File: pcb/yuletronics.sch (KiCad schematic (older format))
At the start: 35 parts, among them IC1 STM32F042F6P6, IC2 MCP1700, IC3 TLV61225, J1 BATT, J2 MICROUSB, P1 SWD_TC, SW1 BOOTLOAD, SW2 PWR_SWITCH

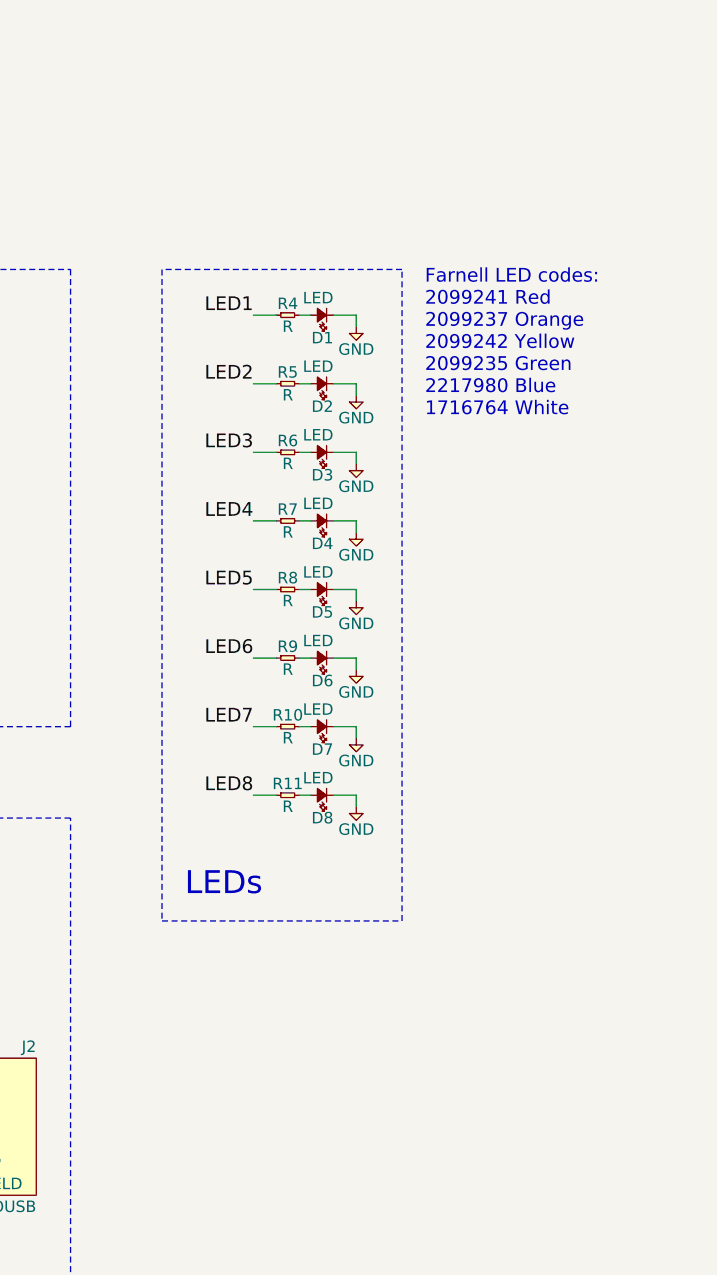
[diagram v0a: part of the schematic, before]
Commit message: More LEDs, MOSFETs, board outline
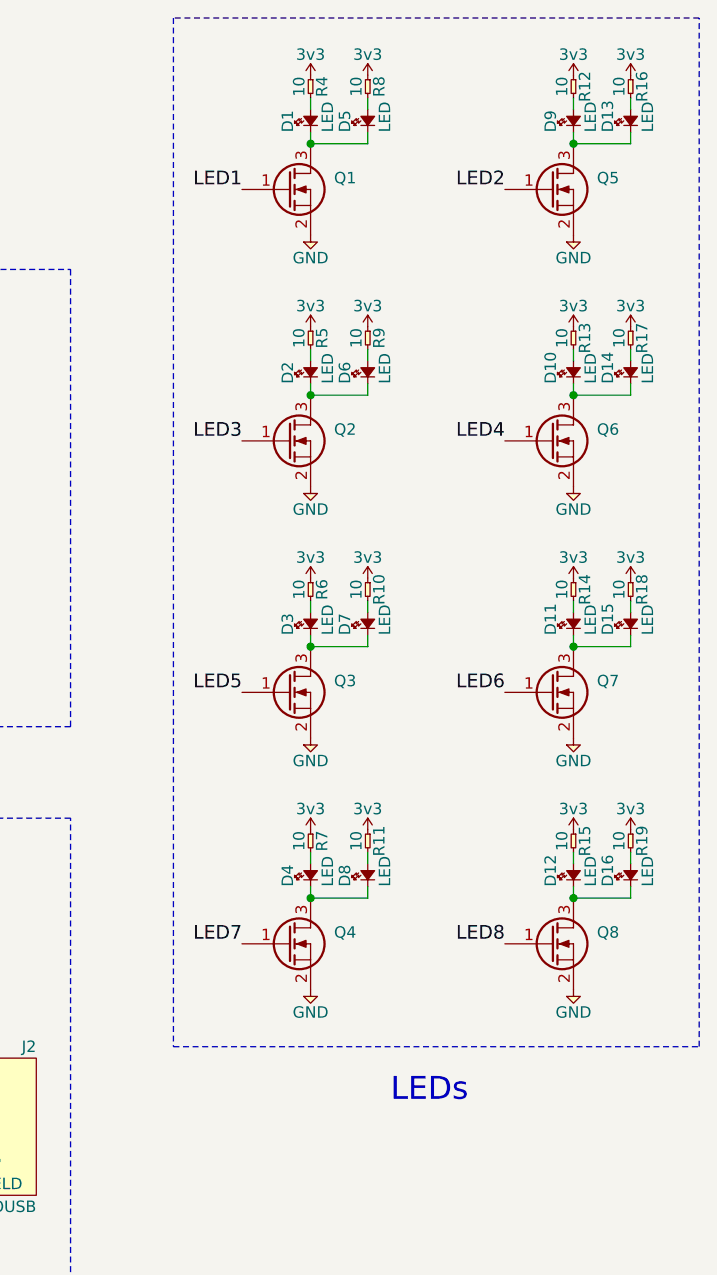
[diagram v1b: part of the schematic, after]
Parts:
- added D10, D11, D12, D13, D14, D15, D16, D9: LED, agg:0805-LED, symbol LED
- added Q1, Q2, Q3, Q4, Q5, Q6, Q7, Q8: BSS138P, agg:SOT-23, symbol Q_NMOS_GSD
- added R12, R13, R14, R15, R16, R17, R18, R19: 10, agg:0805, symbol R
- D1, D3, D5, D7: Farnell 2099241 -> 1716764
- D2, D4, D6, D8: Farnell 2099235 -> 1716764
- R10, R11, R4, R5, R6, R7, R8, R9: value R -> 10; Farnell (none) -> 9332421
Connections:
- net 3v3: now also R10.1, R11.1, R4.1, R5.1, R6.1, R7.1, R8.1, R9.1, R12.1, R13.1, R14.1, R15.1, R16.1, R17.1, R18.1, R19.1
- net GND: now also Q1.2 (S), Q2.2 (S), Q3.2 (S), Q4.2 (S), Q5.2 (S), Q6.2 (S), Q7.2 (S), Q8.2 (S); no longer D1.1, D2.1, D3.1, D4.1, D5.1, D6.1, D7.1, D8.1
- net LED1: now also Q1.1 (G); no longer R4.1
- net LED2: now also Q5.1 (G); no longer R5.1
- net LED3: now also Q2.1 (G); no longer R6.1
- net LED4: now also Q6.1 (G); no longer R7.1
- net LED5: now also Q3.1 (G); no longer R8.1
- net LED6: now also Q7.1 (G); no longer R9.1
- net LED7: now also Q4.1 (G); no longer R10.1
- net LED8: now also Q8.1 (G); no longer R11.1
- new net: D1.1, D5.1, Q1.3 (D)
- new net: D13.1, D9.1, Q5.3 (D)
- new net: D9.2, R12.2
- new net: D13.2, R16.2
- new net: D2.1, D6.1, Q2.3 (D)
- new net: D10.1, D14.1, Q6.3 (D)
- new net: D10.2, R13.2
- new net: D14.2, R17.2
- new net: D3.1, D7.1, Q3.3 (D)
- new net: D11.1, D15.1, Q7.3 (D)
- new net: D11.2, R14.2
- new net: D15.2, R18.2
- new net: D4.1, D8.1, Q4.3 (D)
- new net: D12.1, D16.1, Q8.3 (D)
- new net: D12.2, R15.2
- new net: D16.2, R19.2
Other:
- note removed: "Farnell LED codes:\n2099241 Red\n2099237 Orange\n2099242 Yellow\n2099235 Green\n2217980 Blue\n1716764 White"
- moved on the sheet: D1, R4

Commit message: Partially did new 5V bus
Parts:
- removed IC3: TLV61225, agg:SC-70-6, symbol TLV61225
- removed SW2: PWR_SWITCH, agg:SPDT_SWITCH, symbol SWITCH_SPDT
- added IC?: TLV61220, agg:SOT-23-6, symbol TLV61220
- added R? (x2): R, symbol R
- added U1: dpdt, agg:dpdt, symbol dpdt
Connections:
- net USB_3V3 is gone; now on net 3v3: C6.1, IC2.2 (VOUT)
- net 5v: now also U1.5; no longer J2.1 (VCC), R2.1
- net GND: now also IC?.2 (GND), R?.2
- net VBATT: now also IC?.3 (EN), IC?.6 (VBAT), U1.2; no longer J1.2
- net at L1.2: now also IC?.1 (SW)
- net BATT_3V3 renamed BATT_5V
- net BATT_5V: now also IC?.5 (VOUT), R?.1, U1.4
- new net: J1.2, U1.1
- new net: IC?.4 (FB), R?.1, R?.2
- new net USB_5V: J2.1 (VCC), R2.1, U1.6
- no-connect marks 7 -> 8
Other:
- moved on the sheet: C4, C5, C6, C7, IC2, J1, L1

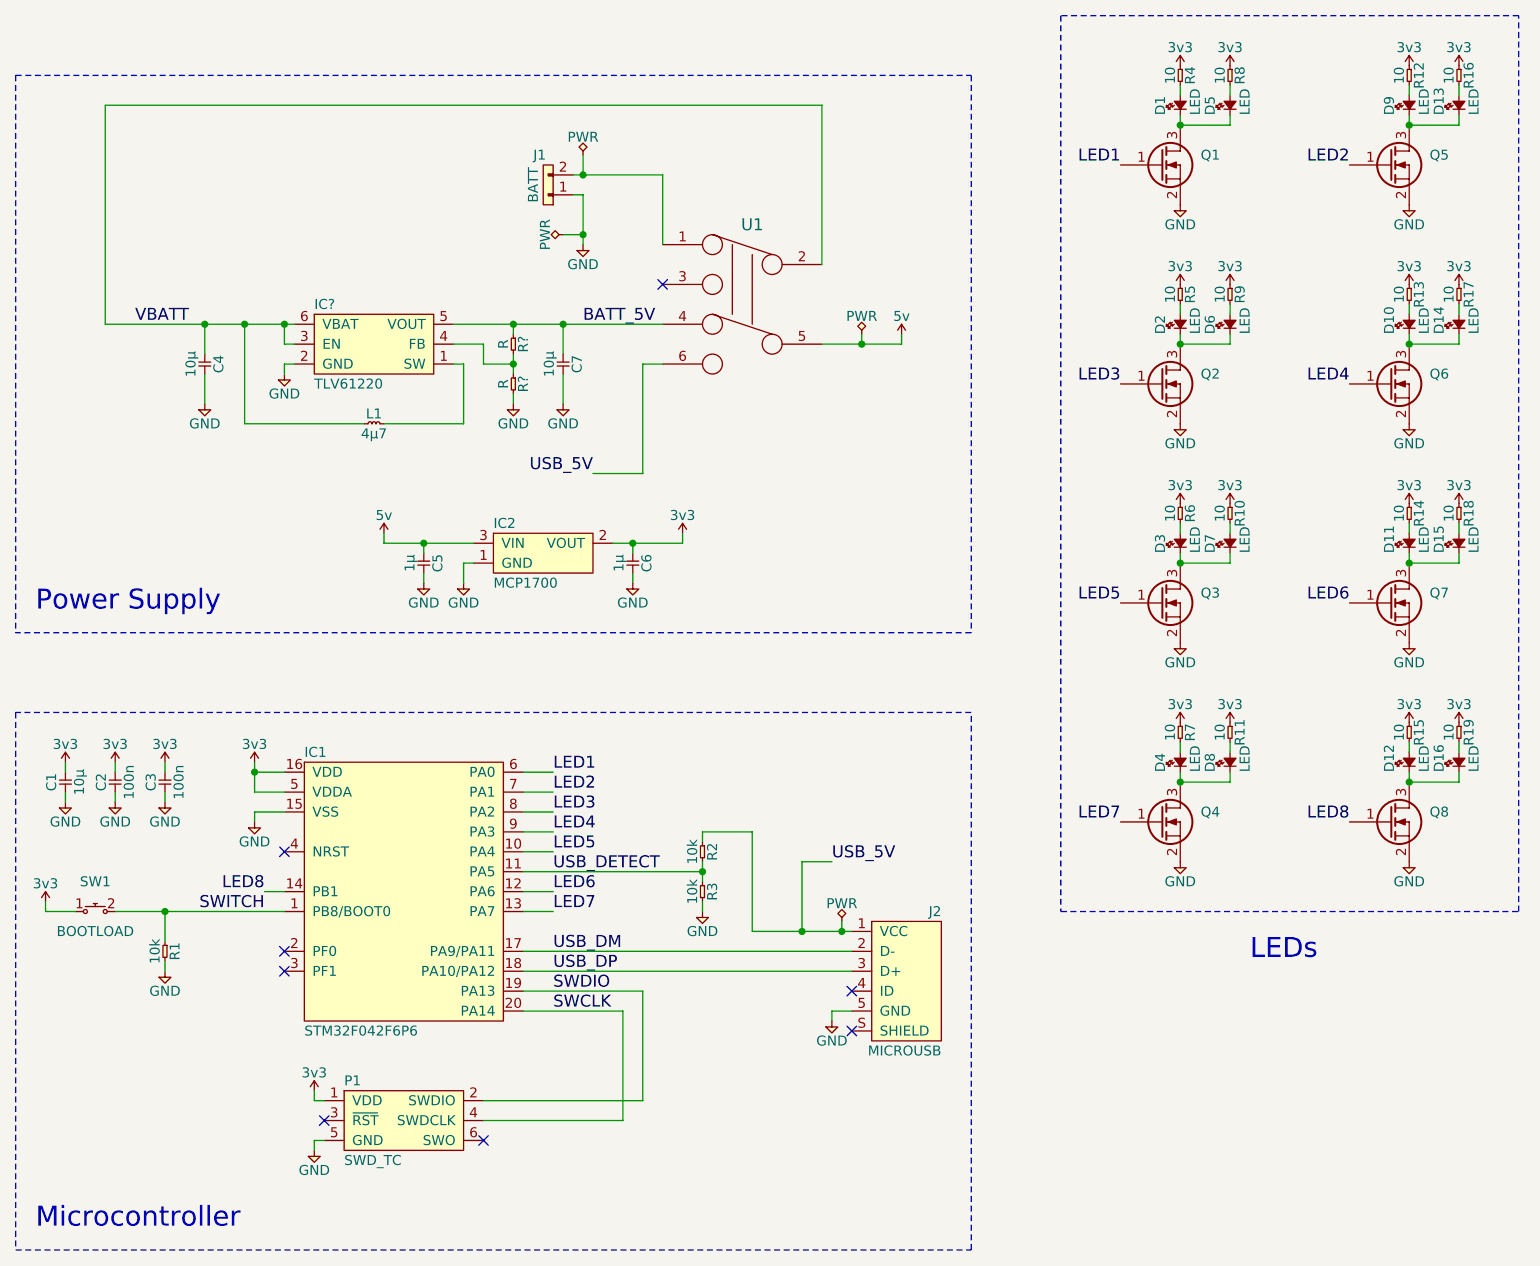
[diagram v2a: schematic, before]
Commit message: Added FET pulldowns, placed and routed
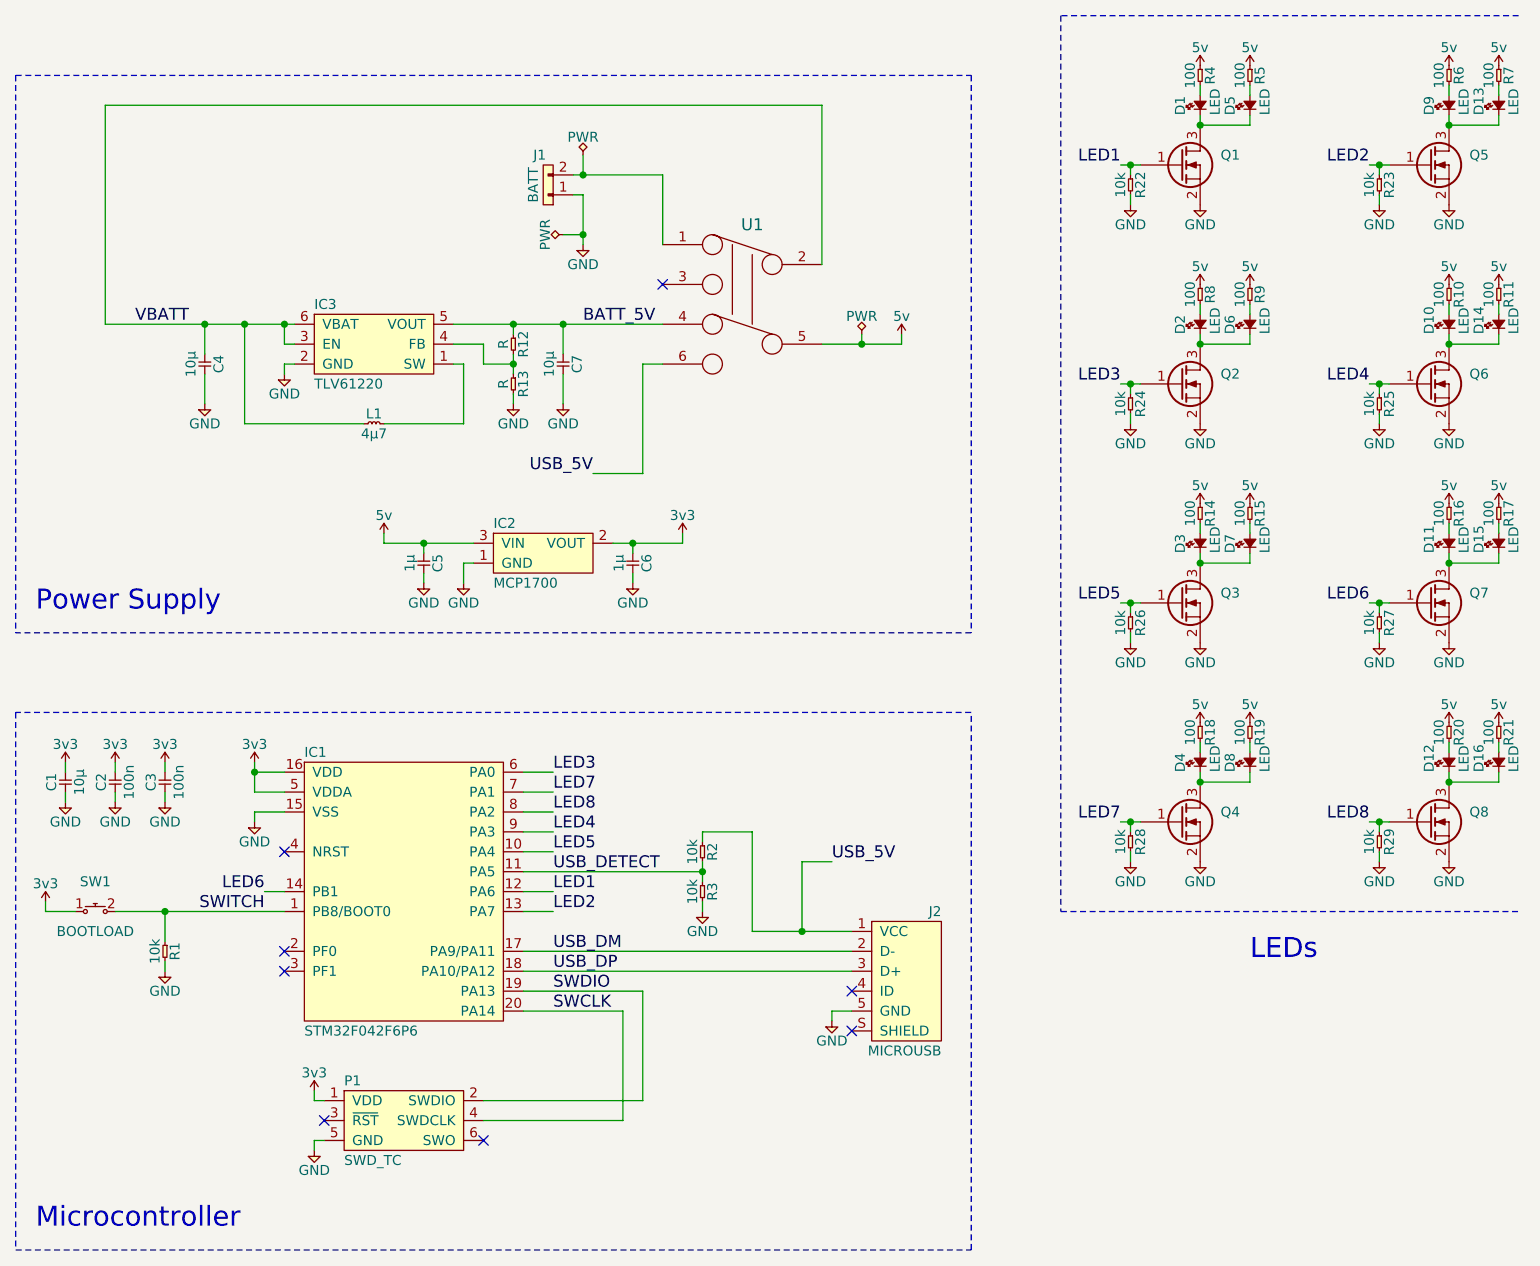
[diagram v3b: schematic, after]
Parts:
- removed R12, R13: 10, agg:0805, symbol R
- added R20, R21: 100, agg:0805, symbol R
- added R22, R23, R24, R25, R26, R27, R28, R29: 10k, agg:0805, symbol R
- R10, R11, R14, R15, R16, R17, R18, R19, R4, R5, R6, R7, R8, R9: value 10 -> 100; Farnell 9332421 -> (none)
- R12, R13: renamed from R?; footprint (none) -> agg:0805
- gave numbers to parts that had none: 1
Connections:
- net 3v3: no longer R10.1, R11.1, R14.1, R15.1, R16.1, R17.1, R18.1, R19.1, R4.1, R5.1, R6.1, R7.1, R8.1, R9.1
- net 5v: now also R10.1, R11.1, R14.1, R15.1, R16.1, R17.1, R18.1, R19.1, R4.1, R5.1, R6.1, R7.1, R8.1, R9.1, R20.1, R21.1
- net GND: now also R22.2, R23.2, R24.2, R25.2, R26.2, R27.2, R28.2, R29.2
- net LED1: now also IC1.12 (PA6), R22.1; no longer IC1.6 (PA0)
- net LED2: now also IC1.13 (PA7), R23.1; no longer IC1.7 (PA1)
- net LED3: now also IC1.6 (PA0), R24.1; no longer IC1.8 (PA2)
- net LED4: now also R25.1
- net LED5: now also R26.1
- net LED6: now also IC1.14 (PB1), R27.1; no longer IC1.12 (PA6)
- net LED7: now also IC1.7 (PA1), R28.1; no longer IC1.13 (PA7)
- net LED8: now also IC1.8 (PA2), R29.1; no longer IC1.14 (PB1)
- net at D5.2: now also R5.2; no longer R8.2
- net at D9.2: now also R6.2
- net at D13.2: now also R7.2; no longer R16.2
- net at D2.2: now also R8.2; no longer R5.2
- net at D10.2: now also R10.2
- net at D14.2: now also R11.2; no longer R17.2
- net at D3.2: now also R14.2; no longer R6.2
- net at D7.2: now also R15.2; no longer R10.2
- net at D11.2: now also R16.2; no longer R14.2
- net at D15.2: now also R17.2; no longer R18.2
- net at D4.2: now also R18.2; no longer R7.2
- net at D8.2: now also R19.2; no longer R11.2
- net at D12.2: now also R20.2; no longer R15.2
- net at D16.2: now also R21.2; no longer R19.2
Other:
- moved on the sheet: D1, D10, D11, D12, D13, D14, D15, D16, D2, D3, D4, D5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

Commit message: ERC/DRC
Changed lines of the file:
@@
 	8200 4750 8300 4750
 Connection ~ 8250 4750
+$Comp
+L PWR #FLG061
+U 1 1 581D0A3F
+P 2450 2150
+F 0 "#FLG061" H 2450 2310 50  0001 C CNN
+F 1 "PWR" H 2450 2240 50  0000 C CNN
+F 2 "" H 2450 2150 50  0001 C CNN
+F 3 "" H 2450 2150 50  0001 C CNN
+	1    2450 2150
+	1    0    0    -1
+$EndComp
+Wire Wire Line
+	2450 2150 2450 2250
+Connection ~ 2450 2250
 $EndSCHEMATC

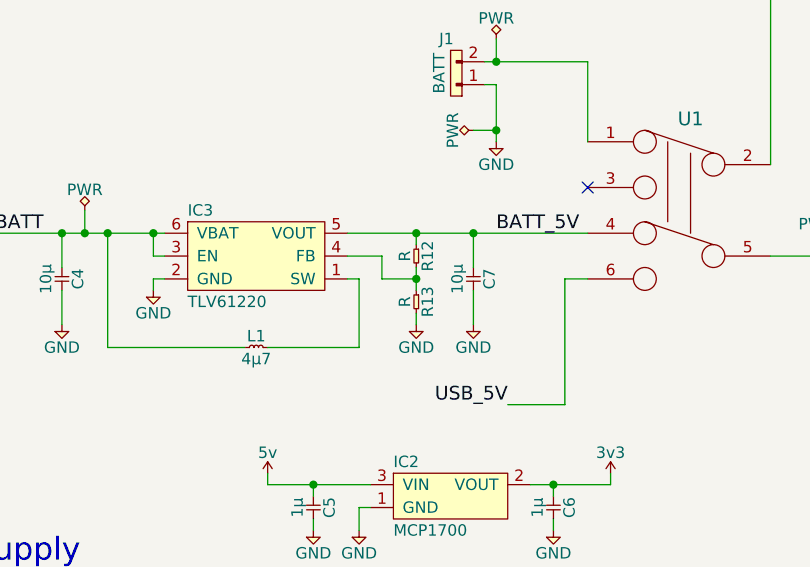
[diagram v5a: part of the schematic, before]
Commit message: Added stencil, SMPS R values/parts
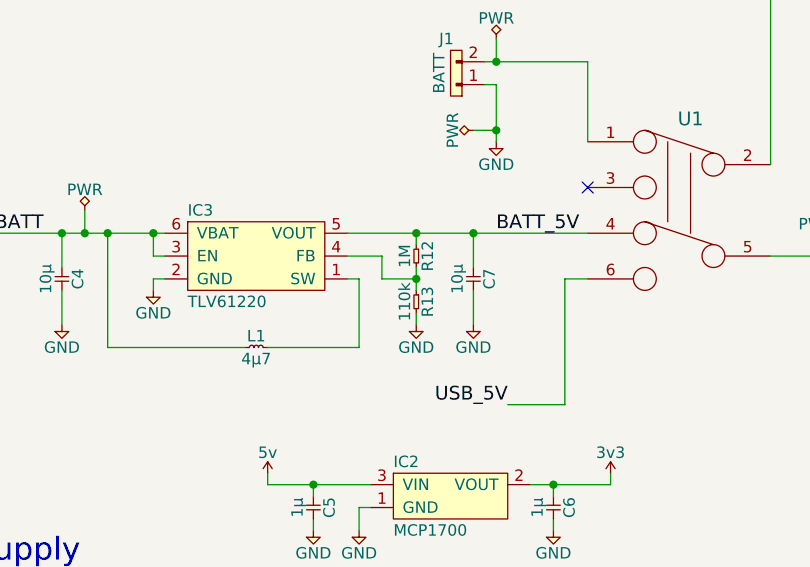
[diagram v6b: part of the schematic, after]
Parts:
- R12: value R -> 1M; Farnell (none) -> 9332413
- R13: value R -> 110k; Farnell (none) -> 9332464
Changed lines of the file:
@@
 P 3900 2300
 F 0 "R12" H 3950 2350 50  0000 C CNN
-F 1 "R" H 3950 2250 50  0000 C CNN
+F 1 "1M" H 3950 2250 50  0000 C CNN
 F 2 "agg:0805" H 3900 2300 50  0001 C CNN
 F 3 "" H 3900 2300 50  0001 C CNN
+F 4 "9332413" H 3900 2300 60  0001 C CNN "Farnell"
 	1    3900 2300
 	0    1    1    0
@@
 P 3900 2500
 F 0 "R13" H 3950 2550 50  0000 C CNN
-F 1 "R" H 3950 2450 50  0000 C CNN
+F 1 "110k" H 3950 2450 50  0000 C CNN
 F 2 "agg:0805" H 3900 2500 50  0001 C CNN
 F 3 "" H 3900 2500 50  0001 C CNN
+F 4 "9332464" H 3900 2500 60  0001 C CNN "Farnell"
 	1    3900 2500
 	0    1    1    0

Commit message: Updated BOM
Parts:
- R22, R23, R24, R25, R26, R27, R28, R29: Farnell (none) -> 9332391
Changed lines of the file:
@@
 LIBS:dpdt
 LIBS:tlv61220
-LIBS:switch
 LIBS:yuletronics-cache
 EELAYER 25 0
@@
 F 2 "agg:0805" H 7000 2600 50  0001 C CNN
 F 3 "" H 7000 2600 50  0001 C CNN
+F 4 "9332391" H 7000 2600 60  0001 C CNN "Farnell"
 	1    7000 2600
 	0    1    1    0
@@
 F 2 "agg:0805" H 7000 1500 50  0001 C CNN
 F 3 "" H 7000 1500 50  0001 C CNN
+F 4 "9332391" H 7000 1500 60  0001 C CNN "Farnell"
 	1    7000 1500
 	0    1    1    0
@@
 F 2 "agg:0805" H 7000 3700 50  0001 C CNN
 F 3 "" H 7000 3700 50  0001 C CNN
+F 4 "9332391" H 7000 3700 60  0001 C CNN "Farnell"
 	1    7000 3700
 	0    1    1    0
@@
 F 2 "agg:0805" H 7000 4800 50  0001 C CNN
 F 3 "" H 7000 4800 50  0001 C CNN
+F 4 "9332391" H 7000 4800 60  0001 C CNN "Farnell"
 	1    7000 4800
 	0    1    1    0
@@
 F 2 "agg:0805" H 8250 1500 50  0001 C CNN
 F 3 "" H 8250 1500 50  0001 C CNN
+F 4 "9332391" H 8250 1500 60  0001 C CNN "Farnell"
 	1    8250 1500
 	0    1    1    0
@@
 F 2 "agg:0805" H 8250 2600 50  0001 C CNN
 F 3 "" H 8250 2600 50  0001 C CNN
+F 4 "9332391" H 8250 2600 60  0001 C CNN "Farnell"
 	1    8250 2600
 	0    1    1    0
@@
 F 2 "agg:0805" H 8250 3700 50  0001 C CNN
 F 3 "" H 8250 3700 50  0001 C CNN
+F 4 "9332391" H 8250 3700 60  0001 C CNN "Farnell"
 	1    8250 3700
 	0    1    1    0
@@
 F 2 "agg:0805" H 8250 4800 50  0001 C CNN
 F 3 "" H 8250 4800 50  0001 C CNN
+F 4 "9332391" H 8250 4800 60  0001 C CNN "Farnell"
 	1    8250 4800
 	0    1    1    0
